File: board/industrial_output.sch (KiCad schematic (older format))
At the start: 3 parts, among them Q1501 NJT4031NT1G

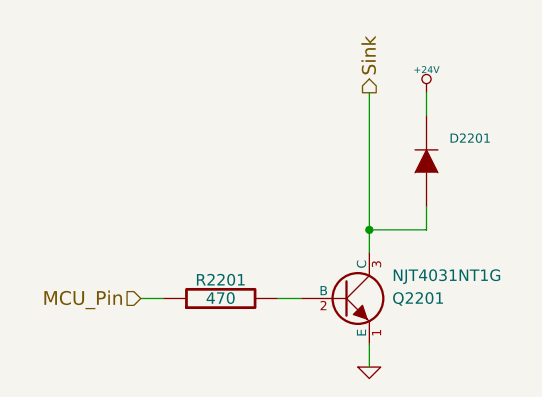
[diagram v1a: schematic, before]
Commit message: No more airwires
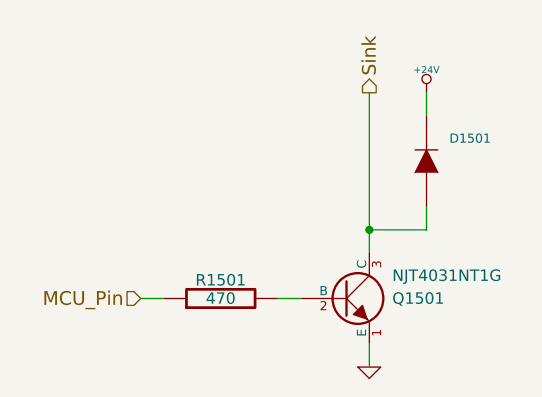
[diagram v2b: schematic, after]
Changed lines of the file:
@@
 AR Path="/52FAF275/52E6FDE0" Ref="Q2101"  Part="1"
 AR Path="/52FAF279/52E6FDE0" Ref="Q2201"  Part="1"
-F 0 "Q2201" H 5650 4500 50  0000 L CNN
+F 0 "Q1501" H 5650 4500 50  0000 L CNN
 F 1 "NJT4031NT1G" H 5650 4600 50  0000 L CNN
 F 2 "" H 5450 4500 60  0000 C CNN
@@
 AR Path="/52FAF275/52E6FDF4" Ref="R2101"  Part="1"
 AR Path="/52FAF279/52E6FDF4" Ref="R2201"  Part="1"
-F 0 "R2201" V 4980 4500 50  0000 C CNN
+F 0 "R1501" V 4980 4500 50  0000 C CNN
 F 1 "470" V 4900 4500 50  0000 C CNN
 F 2 "" H 4900 4500 60  0000 C CNN
@@
 AR Path="/52FAF275/52E705F0" Ref="D2101"  Part="1"
 AR Path="/52FAF279/52E705F0" Ref="D2201"  Part="1"
-F 0 "D2201" V 5900 3800 40  0000 R CNN
+F 0 "D1501" V 5900 3800 40  0000 R CNN
 F 1 "RSX501L-20TE25" V 5800 3800 40  0001 R CNN
 F 2 "" H 5800 3900 60  0000 C CNN
